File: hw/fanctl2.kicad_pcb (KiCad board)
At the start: 2 copper layers, 80 x 64.8 mm, 0 parts

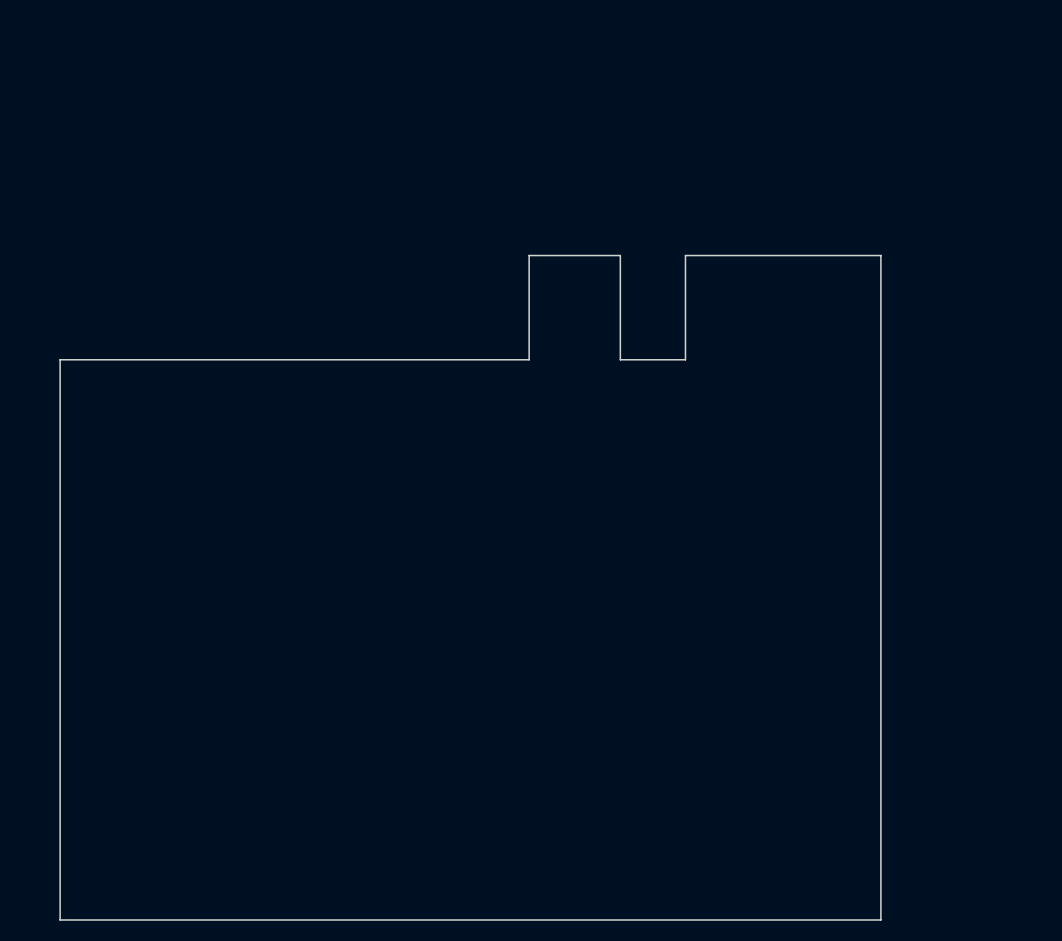
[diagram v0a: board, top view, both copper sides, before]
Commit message: PCB pretty much done.
I changed the size so it would be smaller than 10x10 cm, otherwise it's
absurdly expensive to have it made.
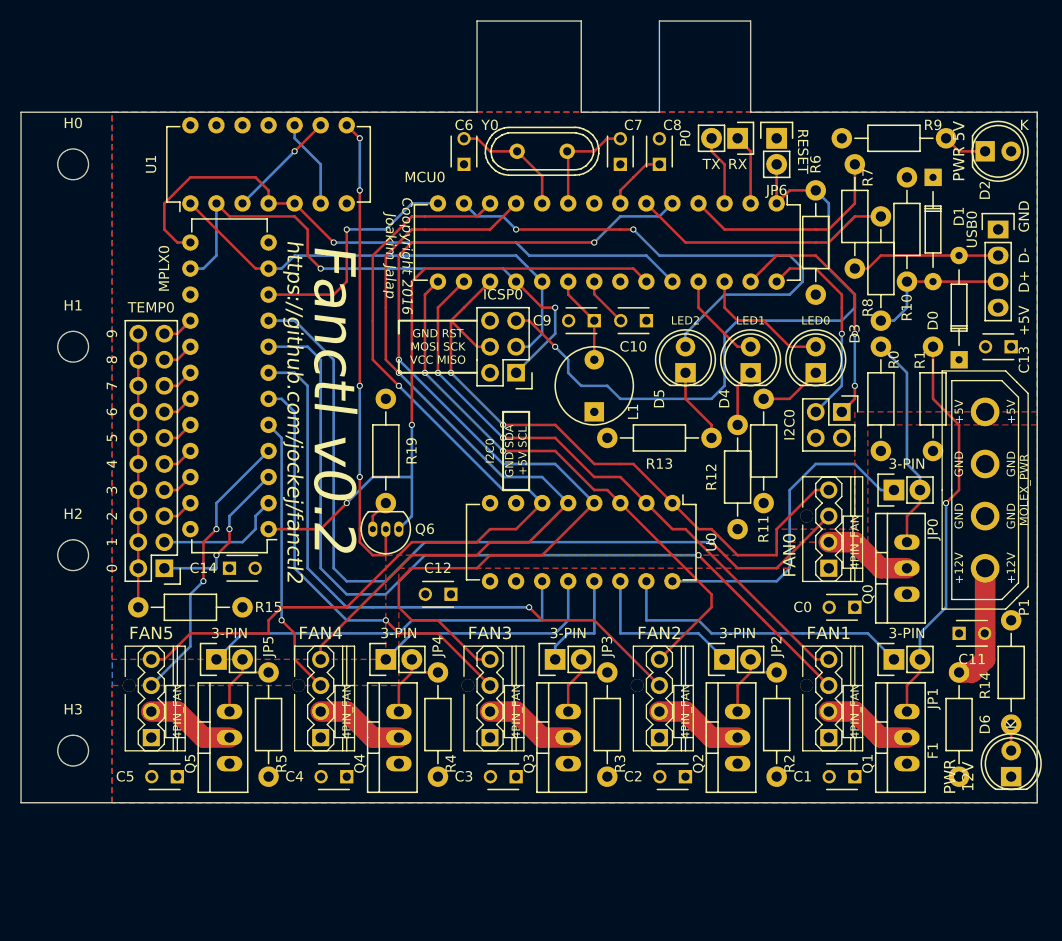
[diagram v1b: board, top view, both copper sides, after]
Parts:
- added C0: Decoupler, Capacitors_ThroughHole:C_Disc_D3_P2.5, F.Cu at (133.3, 130.8)
- added C1: Decoupler, Capacitors_ThroughHole:C_Disc_D3_P2.5, F.Cu at (133.3, 147.3)
- added C10: Decoupler, Capacitors_ThroughHole:C_Disc_D3_P2.5, F.Cu at (113.0, 102.9)
- added C11: Decoupler, Capacitors_ThroughHole:C_Disc_D3_P2.5, F.Cu at (143.5, 133.3)
- added C12: Decoupler, Capacitors_ThroughHole:C_Disc_D3_P2.5, F.Cu at (94.0, 129.5)
- added C13: Decoupler, Capacitors_ThroughHole:C_Disc_D3_P2.5, F.Cu at (148.6, 105.4)
- added C14: Decoupler, Capacitors_ThroughHole:C_Disc_D3_P2.5, F.Cu at (72.4, 127.0)
- added C2: Decoupler, Capacitors_ThroughHole:C_Disc_D3_P2.5, F.Cu at (116.8, 147.3)
- added C3: Decoupler, Capacitors_ThroughHole:C_Disc_D3_P2.5, F.Cu at (100.3, 147.3)
- added C4: Decoupler, Capacitors_ThroughHole:C_Disc_D3_P2.5, F.Cu at (83.8, 147.3)
- added C5: Decoupler, Capacitors_ThroughHole:C_Disc_D3_P2.5, F.Cu at (67.3, 147.3)
- added C6: Decoupler, Capacitors_ThroughHole:C_Disc_D3_P2.5, F.Cu at (95.2, 87.6)
- added C7: Decoupler, Capacitors_ThroughHole:C_Disc_D3_P2.5, F.Cu at (110.5, 87.6)
- added C8: Decoupler, Capacitors_ThroughHole:C_Disc_D3_P2.5, F.Cu at (114.3, 87.6)
- added C9: Decoupler, Capacitors_ThroughHole:C_Disc_D3_P2.5, F.Cu at (108.0, 102.9)
- added D0: ZENER, Diodes_ThroughHole:Diode_DO-35_SOD27_Horizontal_RM10, F.Cu at (143.5, 106.7)
- added D1: ZENER, Diodes_ThroughHole:Diode_DO-35_SOD27_Horizontal_RM10, F.Cu at (141.0, 88.9)
- added D2: LED, LEDs:LED-5MM, F.Cu at (146.1, 86.4)
- added D3: LED, LEDs:LED-5MM, F.Cu at (129.5, 108.0)
- added D4: LED, LEDs:LED-5MM, F.Cu at (123.2, 108.0)
- added D5: LED, LEDs:LED-5MM, F.Cu at (116.8, 108.0)
- added D6: LED, LEDs:LED-5MM, F.Cu at (148.6, 147.3)
- added F1: F_Small, Resistors_ThroughHole:Resistor_Horizontal_RM10mm, F.Cu at (143.5, 142.2)
- added FAN0: 4PIN_FAN, ab2_header:AB2_HDR_M04-1V_CPU_FAN, F.Cu at (130.8, 123.2)
- added FAN1: 4PIN_FAN, ab2_header:AB2_HDR_M04-1V_CPU_FAN, F.Cu at (130.8, 139.7)
- added FAN2: 4PIN_FAN, ab2_header:AB2_HDR_M04-1V_CPU_FAN, F.Cu at (114.3, 139.7)
- added FAN3: 4PIN_FAN, ab2_header:AB2_HDR_M04-1V_CPU_FAN, F.Cu at (97.8, 139.7)
- added FAN4: 4PIN_FAN, ab2_header:AB2_HDR_M04-1V_CPU_FAN, F.Cu at (81.3, 139.7)
- added FAN5: 4PIN_FAN, ab2_header:AB2_HDR_M04-1V_CPU_FAN, F.Cu at (64.8, 139.7)
- added H0: MountingHole_3mm, Mounting_Holes:MountingHole_3mm, F.Cu at (57.1, 87.6)
- added H1: MountingHole_3mm, Mounting_Holes:MountingHole_3mm, F.Cu at (57.1, 105.4)
- added H2: MountingHole_3mm, Mounting_Holes:MountingHole_3mm, F.Cu at (57.1, 125.7)
- added H3: MountingHole_3mm, Mounting_Holes:MountingHole_3mm, F.Cu at (57.1, 144.8)
- added I2C0: I2C_HDR, Pin_Headers:Pin_Header_Straight_2x02, F.Cu at (132.1, 111.8)
- added ICSP0: Prog_con, Pin_Headers:Pin_Header_Straight_2x03, F.Cu at (100.3, 108.0)
- added JP0: Jumper_NC_Small, Pin_Headers:Pin_Header_Straight_1x02, F.Cu at (137.2, 119.4)
- added JP1: Jumper_NC_Small, Pin_Headers:Pin_Header_Straight_1x02, F.Cu at (137.2, 135.9)
- added JP2: Jumper_NC_Small, Pin_Headers:Pin_Header_Straight_1x02, F.Cu at (120.7, 135.9)
- added JP3: Jumper_NC_Small, Pin_Headers:Pin_Header_Straight_1x02, F.Cu at (104.1, 135.9)
- added JP4: Jumper_NC_Small, Pin_Headers:Pin_Header_Straight_1x02, F.Cu at (87.6, 135.9)
- added JP5: Jumper_NC_Small, Pin_Headers:Pin_Header_Straight_1x02, F.Cu at (71.1, 135.9)
- added JP6: Jumper_NO_Small, Pin_Headers:Pin_Header_Straight_1x02, F.Cu at (125.7, 85.1)
- added L1: INDUCTOR_SMALL, Inductors:INDUCTOR_V, F.Cu at (108.0, 109.2)
- added MCU0: ATMEGA168PA-P, Housings_DIP:DIP-28_W7.62mm, F.Cu at (125.7, 91.4)
- added MPLX0: Multiplexer_16:1, Housings_DIP:DIP-24_W7.62mm, F.Cu at (76.2, 123.2)
- added P0: CONN_01X02, Pin_Headers:Pin_Header_Straight_1x02, F.Cu at (121.9, 85.1)
- added P1: MOLEX_PWR, ab2_power:AB2_ATX_PSU-4PIN-V, F.Cu at (146.1, 119.4)
- added Q0: FAN_PMOS, TO_SOT_Packages_THT:TO-220_Neutral123_Vertical, F.Cu at (138.4, 127.0)
- added Q1: FAN_PMOS, TO_SOT_Packages_THT:TO-220_Neutral123_Vertical, F.Cu at (138.4, 143.5)
- added Q2: FAN_PMOS, TO_SOT_Packages_THT:TO-220_Neutral123_Vertical, F.Cu at (121.9, 143.5)
- added Q3: FAN_PMOS, TO_SOT_Packages_THT:TO-220_Neutral123_Vertical, F.Cu at (105.4, 143.5)
- added Q4: FAN_PMOS, TO_SOT_Packages_THT:TO-220_Neutral123_Vertical, F.Cu at (88.9, 143.5)
- added Q5: FAN_PMOS, TO_SOT_Packages_THT:TO-220_Neutral123_Vertical, F.Cu at (72.4, 143.5)
- added Q6: BC413, TO_SOT_Packages_THT:TO-92_Inline_Narrow_Oval, F.Cu at (88.9, 123.2)
- added R0: FANCTL2_R, Resistors_ThroughHole:Resistor_Horizontal_RM10mm, F.Cu at (135.9, 110.5)
- added R1: FANCTL2_R, Resistors_ThroughHole:Resistor_Horizontal_RM10mm, F.Cu at (141.0, 110.5)
- added R10: FANCTL2_R, Resistors_ThroughHole:Resistor_Horizontal_RM10mm, F.Cu at (138.4, 94.0)
- added R11: FANCTL2_R, Resistors_ThroughHole:Resistor_Horizontal_RM10mm, F.Cu at (124.5, 115.6)
- added R12: FANCTL2_R, Resistors_ThroughHole:Resistor_Horizontal_RM10mm, F.Cu at (121.9, 118.1)
- added R13: FANCTL2_R, Resistors_ThroughHole:Resistor_Horizontal_RM10mm, F.Cu at (114.3, 114.3)
- added R14: FANCTL2_R, Resistors_ThroughHole:Resistor_Horizontal_RM10mm, F.Cu at (148.6, 137.2)
- added R15: FANCTL2_R, Resistors_ThroughHole:Resistor_Horizontal_RM10mm, F.Cu at (68.6, 130.8)
- added R19: FANCTL2_R, Resistors_ThroughHole:Resistor_Horizontal_RM10mm, F.Cu at (87.6, 115.6)
- added R2: FANCTL2_R, Resistors_ThroughHole:Resistor_Horizontal_RM10mm, F.Cu at (125.7, 142.2)
- added R3: FANCTL2_R, Resistors_ThroughHole:Resistor_Horizontal_RM10mm, F.Cu at (109.2, 142.2)
- added R4: FANCTL2_R, Resistors_ThroughHole:Resistor_Horizontal_RM10mm, F.Cu at (92.7, 142.2)
- added R5: FANCTL2_R, Resistors_ThroughHole:Resistor_Horizontal_RM10mm, F.Cu at (76.2, 142.2)
- added R6: FANCTL2_R, Resistors_ThroughHole:Resistor_Horizontal_RM10mm, F.Cu at (129.5, 95.2)
- added R7: FANCTL2_R, Resistors_ThroughHole:Resistor_Horizontal_RM10mm, F.Cu at (133.3, 92.7)
- added R8: FANCTL2_R, Resistors_ThroughHole:Resistor_Horizontal_RM10mm, F.Cu at (135.9, 97.8)
- added R9: FANCTL2_R, Resistors_ThroughHole:Resistor_Horizontal_RM10mm, F.Cu at (137.2, 85.1)
- added TEMP0: TMP_SNSR_HDR, Pin_Headers:Pin_Header_Straight_2x10, F.Cu at (66.0, 127.0)
- added U0: ULN2003, Housings_DIP:DIP-16_W7.62mm, F.Cu at (115.6, 120.7)
- added U1: 7400, Housings_DIP:DIP-14_W7.62mm, F.Cu at (68.6, 91.4)
- added USB0: USB_HDR, Pin_Headers:Pin_Header_Straight_1x04, F.Cu at (147.3, 94.0)
- added Y0: Crystal_Small, Crystals:Crystal_HC49-U_Vertical, F.Cu at (102.9, 86.4)
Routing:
- net PWM3: track 0.00 -> 99.5 mm, vias 0 -> 2
- net PWM5: track 0.00 -> 91.1 mm, vias 0 -> 1
- net TACH1: track 0.00 -> 83.3 mm, vias 0 -> 1
- net TACH0: track 0.00 -> 81.8 mm, vias 0 -> 1
- net PWM4: track 0.00 -> 79.7 mm, vias 0 -> 1
- net Net-(ICSP0-Pad5): track 0.00 -> 64.7 mm, vias 0 -> 1
- net SENS0: track 0.00 -> 64.6 mm, vias 0 -> 2
- net PWM0: track 0.00 -> 63.6 mm, vias 0 -> 2
- net TACH2: track 0.00 -> 61.1 mm, vias 0 -> 1
- net SEL3: track 0.00 -> 61.1 mm, vias 0 -> 1
- net PWM1: track 0.00 -> 59.6 mm, vias 0 -> 2
- net SEL2: track 0.00 -> 54.8 mm, vias 0 -> 2
- net PWM2: track 0.00 -> 54.8 mm, vias 0 -> 2
- net LED2: track 0.00 -> 51.7 mm, vias 0 -> 2
- net Net-(Q6-Pad2): track 0.00 -> 46.8 mm, vias 0 -> 4
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- added copper zone on F.Cu, net +12V
- added copper zone on F.Cu, net +5V
- added copper zone on B.Cu, net GND
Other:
- board size 80 x 64.8 mm -> 99.1 x 76.2 mm
- net class fanpwr added: clearance 0.2, trace_width 2, via_dia 0.8, via_drill 0.5
- rule pad_to_mask_clearance: 0.2 -> 0
- board text added: "+5V"
- board text added: "0"
- board text added: "1"
- board text added: "2"
- board text added: "3"
- board text added: "3-PIN"
- board text added: "4"
- board text added: "5"
- board text added: "6"
- board text added: "7"
- board text added: "8"
- board text added: "9"
- board text added: "Coopyright 2016 Joakim Jalap"
- board text added: "D+"
- board text added: "D-"
- board text added: "Fanctl v0.2"
- board text added: "GND"
- board text added: "GND RST MOSI SCK VCC MISO"
- board text added: "GND SDA +5V SCL"
- board text added: "I2C0"
- board text added: "LED0"
- board text added: "LED1"
- board text added: "LED2"
- board text added: "PWR 12V"
- board text added: "PWR 5V"
- board text added: "RESET"
- board text added: "RX"
- board text added: "TX"
- board text added: "https://github.com/jockej/fanctl2"

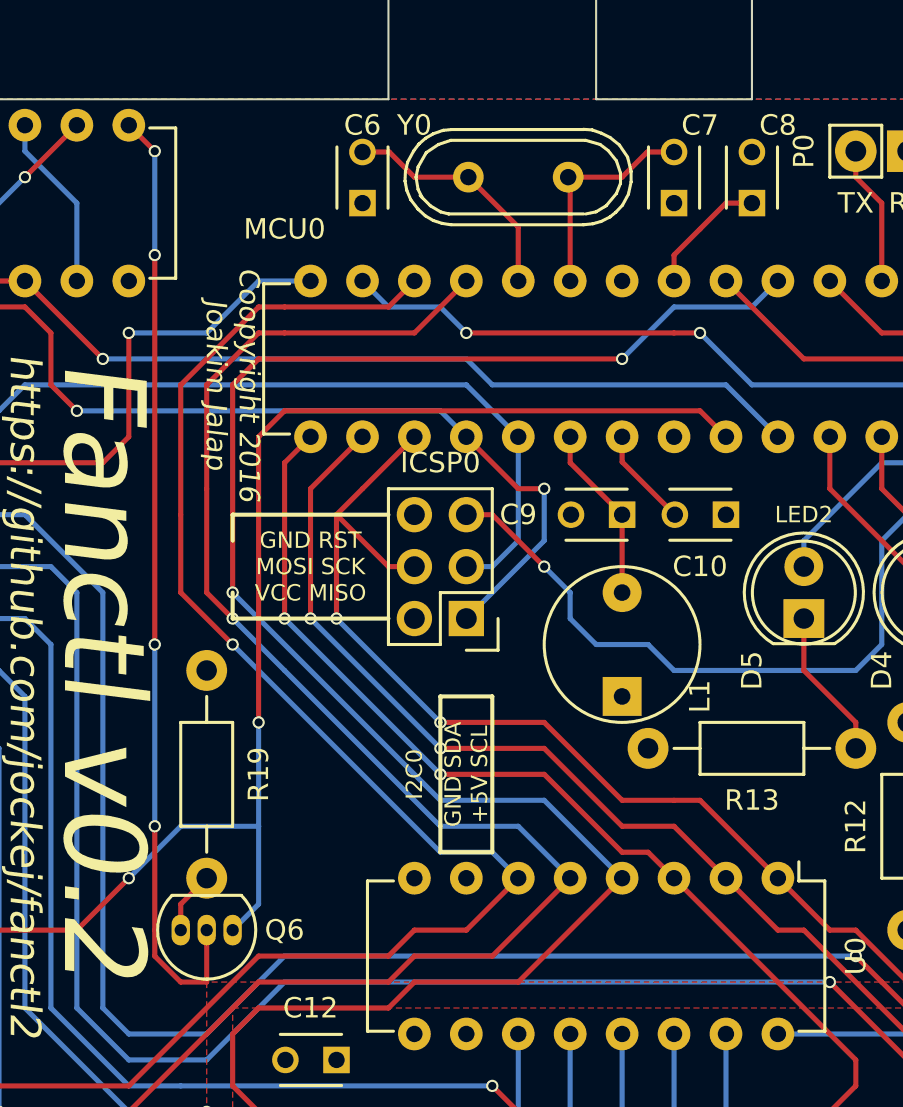
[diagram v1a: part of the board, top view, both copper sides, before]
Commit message: Add a resistor.
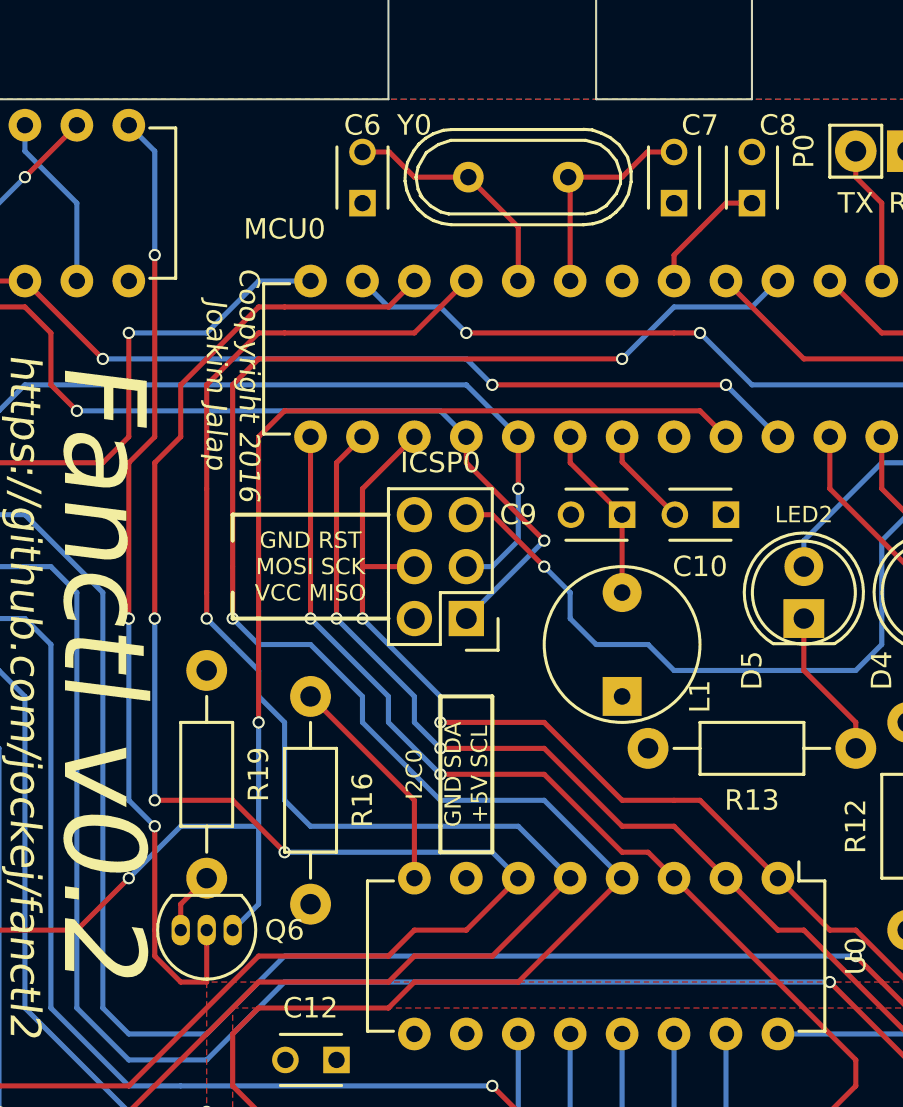
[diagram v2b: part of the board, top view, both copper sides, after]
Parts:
- added R16: R, Resistors_ThroughHole:Resistor_Horizontal_RM10mm, F.Cu at (92.7, 116.8)
- U0: value ULN2003 -> F2_ULN2003
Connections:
- U0 pad 8: GND -> Net-(R16-Pad1)
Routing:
- net Net-(R16-Pad1): track 0.00 -> 11.0 mm
- net PWM5: track 91.1 -> 98.9 mm, vias 1 -> 3
- net PWM4: track 79.7 -> 83.4 mm
- net PWM0: track 63.6 -> 60.3 mm
- net PWM3: track 99.5 -> 101.0 mm
- net PWM1: track 59.6 -> 58.6 mm
- net Net-(Q6-Pad2): track 46.8 -> 47.8 mm, vias 4 -> 3
- net PWM2: track 54.8 -> 53.7 mm
- net SEL2: track 54.8 -> 54.0 mm
- net SEL3: vias 1 -> 3
- net SEL1: vias 0 -> 1

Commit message: Tons of changes
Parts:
- removed Q0: FAN_PMOS, TO_SOT_Packages_THT:TO-220_Neutral123_Vertical
- removed R0: FANCTL2_R, Resistors_ThroughHole:Resistor_Horizontal_RM10mm
- removed TEMP0: TMP_SNSR_HDR, Pin_Headers:Pin_Header_Straight_2x10
- removed U0: F2_ULN2003, Housings_DIP:DIP-16_W7.62mm
- added C15: 22n, Capacitors_ThroughHole:C_Disc_D3_P2.5, F.Cu at (107.3, 87.0)
- added D10: LED, LEDs:LED-5MM, F.Cu at (62.9, 86.4)
- added D11: ZENER, Diodes_ThroughHole:Diode_DO-35_SOD27_Horizontal_RM10, F.Cu at (139.7, 94.6)
- added D12: ZENER, Diodes_ThroughHole:Diode_DO-35_SOD27_Horizontal_RM10, F.Cu at (137.8, 88.9)
- added D7: LED, LEDs:LED-5MM, F.Cu at (142.9, 85.7)
- added D8: LED, LEDs:LED-5MM, F.Cu at (62.9, 101.0)
- added D9: LED, LEDs:LED-5MM, F.Cu at (62.9, 94.0)
- added JP10: JUMPER3, Pin_Headers:Pin_Header_Straight_1x03, F.Cu at (67.3, 132.1)
- added JP11: JUMPER3, Pin_Headers:Pin_Header_Straight_1x03, F.Cu at (62.2, 135.9)
- added JP12: Jumper_NO_Small, Pin_Headers:Pin_Header_Straight_1x02, F.Cu at (120.7, 84.5)
- added JP7: JUMPER3, Pin_Headers:Pin_Header_Straight_1x03, F.Cu at (88.9, 135.9)
- added JP8: JUMPER3, Pin_Headers:Pin_Header_Straight_1x03, F.Cu at (80.6, 132.1)
- added JP9: JUMPER3, Pin_Headers:Pin_Header_Straight_1x03, F.Cu at (75.6, 135.9)
- added P2: CONN_01X04, Pin_Headers:Pin_Header_Straight_1x04, F.Cu at (129.5, 119.4)
- added P3: CONN_01X04, Pin_Headers:Pin_Header_Straight_1x04, F.Cu at (137.2, 119.4)
- added P4: CONN_01X04, Pin_Headers:Pin_Header_Straight_1x04, F.Cu at (133.3, 119.4)
- added Q7: FAN_NMOS, TO_SOT_Packages_THT:TO-220_Neutral123_Vertical, F.Cu at (132.7, 141.0)
- added R17: FANCTL2_R, Resistors_ThroughHole:Resistor_Horizontal_RM10mm, F.Cu at (137.8, 110.5)
- added R18: FANCTL2_R, Resistors_ThroughHole:Resistor_Horizontal_RM10mm, F.Cu at (134.6, 110.5)
- added R20: FANCTL2_R, Resistors_ThroughHole:Resistor_Horizontal_RM10mm, F.Cu at (123.2, 121.9)
- added R21: FANCTL2_R, Resistors_ThroughHole:Resistor_Horizontal_RM10mm, F.Cu at (77.5, 99.1)
- added R22: FANCTL2_R, Resistors_ThroughHole:Resistor_Horizontal_RM10mm, F.Cu at (74.9, 101.0)
- added RR1: RR8, Housings_SIP:SIP9_Housing, F.Cu at (83.2, 115.6)
- added TEMP1: TMP_SNSR_HDR, Pin_Headers:Pin_Header_Straight_2x08, F.Cu at (73.0, 111.8)
- added U2: LM358, Housings_DIP:DIP-8_W7.62mm, F.Cu at (124.5, 99.7)
- added U3: P82B96, Housings_DIP:DIP-8_W7.62mm, F.Cu at (112.4, 118.1)
- C0, C1, C13, C14, C2, C3, C4, C5, C8, C9: value Decoupler -> 0.1u
- C10, C12: value Decoupler -> C
- C6, C7: value Decoupler -> 22p
- D0, D1: value ZENER -> D
- D2, D3, D4, D5: value LED -> D; footprint LEDs:LED-5MM -> Diodes_ThroughHole:Diode_DO-35_SOD27_Horizontal_RM10
- JP0, JP1, JP2, JP3, JP4, JP5: value Jumper_NC_Small -> JUMPER3; footprint Pin_Headers:Pin_Header_Straight_1x02 -> Pin_Headers:Pin_Header_Straight_1x03
- JP6: value Jumper_NO_Small -> JUMPER3; footprint Pin_Headers:Pin_Header_Straight_1x02 -> Pin_Headers:Pin_Header_Straight_1x03
- L1: value INDUCTOR_SMALL -> 10uH
- P0: value CONN_01X02 -> CONN_01X03; footprint Pin_Headers:Pin_Header_Straight_1x02 -> Pin_Headers:Pin_Header_Straight_1x03
- Q1, Q2, Q3, Q4, Q5: value FAN_PMOS -> FAN_NMOS
- R1, R6: value FANCTL2_R -> 10K
- R16: value R -> FANCTL2_R
- R2, R4: value FANCTL2_R -> 10k
- R3, R5: value FANCTL2_R -> R
- R7, R8: value FANCTL2_R -> 68
- moved R1 79.9 mm to (62.2, 123.8), turned to 270 degrees
- moved R5 75.1 mm to (139.7, 102.2), turned to 0 degrees
- moved C5 71.8 mm to (139.1, 148.0), turned to 90 degrees
- moved R15 68.4 mm to (127.0, 95.2), turned to 0 degrees
- moved D2 65.5 mm to (113.0, 142.9), turned to 90 degrees
- moved C0 63.3 mm to (72.4, 148.0), turned to 90 degrees
- moved R11 62.4 mm to (62.2, 110.5)
- moved R12 58.3 mm to (71.1, 89.5), turned to 270 degrees
- moved JP6 56.7 mm to (94.0, 132.1), turned to 270 degrees
- moved D5 56.0 mm to (73.0, 142.9)
- moved D1 55.9 mm to (126.4, 142.9), turned to 90 degrees
- moved R13 52.0 mm to (68.6, 89.5), turned to 90 degrees
- moved D4 50.8 mm to (86.4, 142.9)
- moved I2C0 47.8 mm to (85.1, 102.9)
- moved C1 47.6 mm to (85.7, 148.0), turned to 90 degrees
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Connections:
- C0 pad 2: GND -> 12VGND
- C1 pad 2: GND -> 12VGND
- C10 pad 1: GND -> I5V
- C11 pad 1: GND -> 12VGND
- C12 pad 1: +12V -> Net-(C12-Pad1)
- C12 pad 2: GND -> I12V
- C13 pad 1: +5V -> Net-(C13-Pad1)
- C2 pad 2: GND -> 12VGND
- C3 pad 2: GND -> 12VGND
- C4 pad 2: GND -> 12VGND
- C5 pad 2: GND -> 12VGND
- D0 pad 1: GND -> Net-(D0-Pad1)
- D0 pad 2: Net-(D0-Pad2) -> 12VGND
- D1 pad 1: GND -> Net-(D1-Pad1)
- D1 pad 2: Net-(D1-Pad2) -> 12VGND
- D2 pad 2: +5V -> 12VGND
- D3 pad 2: LED0 -> 12VGND
- D4 pad 2: LED1 -> 12VGND
- D5 pad 2: LED2 -> 12VGND
- D6 pad 1: GND -> 12VGND
- FAN0 pad 1: GND -> 12VGND
- FAN0 pad 2: Net-(FAN0-Pad2) -> Net-(D0-Pad1)
- FAN0 pad 4: PWM0 -> Net-(FAN0-Pad4)
- FAN1 pad 1: GND -> 12VGND
- FAN1 pad 2: Net-(FAN1-Pad2) -> Net-(D1-Pad1)
- FAN1 pad 4: PWM1 -> Net-(FAN1-Pad4)
- FAN2 pad 1: GND -> 12VGND
- FAN2 pad 2: Net-(FAN2-Pad2) -> Net-(D2-Pad1)
- FAN2 pad 4: PWM2 -> Net-(FAN2-Pad4)
- FAN3 pad 1: GND -> 12VGND
- FAN3 pad 2: Net-(FAN3-Pad2) -> Net-(D3-Pad1)
- FAN3 pad 4: PWM3 -> Net-(FAN3-Pad4)
- FAN4 pad 1: GND -> 12VGND
- FAN4 pad 2: Net-(FAN4-Pad2) -> Net-(D4-Pad1)
- FAN4 pad 4: PWM4 -> Net-(FAN4-Pad4)
- FAN5 pad 1: GND -> 12VGND
- FAN5 pad 2: Net-(FAN5-Pad2) -> Net-(D5-Pad1)
- FAN5 pad 4: PWM5 -> Net-(FAN5-Pad4)
- I2C0 pad 1: Net-(I2C0-Pad1) -> SCL
- I2C0 pad 3: Net-(I2C0-Pad3) -> SDA
- JP0 pad 1: PWM12_0 -> COM5V
- JP0 pad 2: Net-(JP0-Pad2) -> Net-(FAN0-Pad4)
- JP1 pad 1: PWM12_1 -> PWM0
- JP2 pad 1: PWM12_2 -> COM5V
- JP2 pad 2: Net-(JP2-Pad2) -> Net-(FAN1-Pad4)
- JP3 pad 1: PWM12_3 -> PWM1
- JP4 pad 1: PWM12_4 -> COM5V
- JP4 pad 2: Net-(JP4-Pad2) -> Net-(FAN2-Pad4)
- JP5 pad 1: PWM12_5 -> PWM2
- JP6 pad 1: GND -> COM5V
- JP6 pad 2: Net-(ICSP0-Pad5) -> Net-(FAN3-Pad4)
- MCU0 pad 21: Net-(C10-Pad2) -> Net-(C9-Pad1)
- MCU0 pad 27: Net-(I2C0-Pad1) -> SDA
- MCU0 pad 28: Net-(I2C0-Pad3) -> SCL
- MPLX0 pad 16: Net-(MPLX0-Pad16) -> I12V
- MPLX0 pad 17: Net-(MPLX0-Pad17) -> I5V
- P0 pad 1: Net-(MCU0-Pad2) -> Net-(MCU0-Pad3)
- P0 pad 2: Net-(MCU0-Pad3) -> Net-(MCU0-Pad2)
- Q1 pad 1: +12V -> Net-(D1-Pad1)
- Q1 pad 2: Net-(FAN1-Pad2) -> +12V
- Q1 pad 3: Net-(JP1-Pad2) -> Net-(JP3-Pad2)
- Q2 pad 1: +12V -> Net-(D2-Pad1)
- Q2 pad 2: Net-(FAN2-Pad2) -> +12V
- Q2 pad 3: Net-(JP2-Pad2) -> Net-(JP5-Pad2)
- Q3 pad 1: +12V -> Net-(D3-Pad1)
- Q3 pad 2: Net-(FAN3-Pad2) -> +12V
- Q3 pad 3: Net-(JP3-Pad2) -> Net-(JP7-Pad2)
- Q4 pad 1: +12V -> Net-(D4-Pad1)
- Q4 pad 2: Net-(FAN4-Pad2) -> +12V
- Q4 pad 3: Net-(JP4-Pad2) -> Net-(JP9-Pad2)
- Q5 pad 1: +12V -> Net-(D5-Pad1)
- Q5 pad 2: Net-(FAN5-Pad2) -> +12V
- Q5 pad 3: Net-(JP5-Pad2) -> Net-(JP11-Pad2)
- Q6 pad 1: SENS0 -> +5V
- R1 pad 1: +12V -> +5V
- R1 pad 2: Net-(JP1-Pad2) -> COM5V
- R10 pad 1: Net-(D1-Pad2) -> Net-(D11-Pad1)
- R11 pad 2: Net-(D3-Pad1) -> Net-(D8-Pad1)
- R12 pad 2: Net-(D4-Pad1) -> Net-(D9-Pad1)
- R13 pad 2: Net-(D5-Pad1) -> Net-(D10-Pad1)
- R15 pad 1: +5V -> Net-(C10-Pad2)
- R15 pad 2: Net-(R15-Pad2) -> +5V
- R16 pad 1: Net-(R16-Pad1) -> I5V
- R16 pad 2: GND -> Net-(C10-Pad2)
- R19 pad 1: Net-(Q6-Pad3) -> Net-(P2-Pad3)
- R19 pad 2: GND -> +12V
- R2 pad 1: +12V -> +5V
- R2 pad 2: Net-(JP2-Pad2) -> Net-(MPLX0-Pad15)
- R3 pad 1: +12V -> GND
- R3 pad 2: Net-(JP3-Pad2) -> 12VGND
- R4 pad 1: +12V -> GND
- R4 pad 2: Net-(JP4-Pad2) -> Net-(Q6-Pad2)
- R5 pad 1: +12V -> +5V
- R5 pad 2: Net-(JP5-Pad2) -> Net-(C13-Pad1)
- R7 pad 1: Net-(D0-Pad2) -> Net-(D12-Pad1)
- R8 pad 1: Net-(D1-Pad2) -> Net-(D11-Pad1)
- R9 pad 1: Net-(D2-Pad1) -> Net-(D7-Pad1)
- U1 pad 10: Net-(U1-Pad10) -> SEL3
- U1 pad 14: +5V -> VCC
- U1 pad 4: SEL3 -> Net-(U1-Pad3)
- U1 pad 5: SEL3 -> Net-(U1-Pad3)
- U1 pad 6: Net-(U1-Pad10) -> Net-(U1-Pad6)
- U1 pad 9: Net-(U1-Pad3) -> Net-(U1-Pad6)
- USB0 pad 2: Net-(D0-Pad2) -> Net-(D12-Pad1)
- USB0 pad 3: Net-(D1-Pad2) -> Net-(D11-Pad1)
- USB0 pad 4: +5V -> Net-(C13-Pad1)
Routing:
- net PWM0: track 60.3 -> 133.8 mm, vias 2 -> 3
- net SCL: track 0.00 -> 65.6 mm, vias 0 -> 2
- net SDA: track 0.00 -> 60.8 mm, vias 0 -> 2
- net SEL0: track 23.2 -> 75.1 mm, vias 1 -> 5
- net I12V: track 0.00 -> 49.7 mm, vias 0 -> 3
- net I5V: track 0.00 -> 45.2 mm, vias 0 -> 3
- net +5V: track 6.13 -> 49.2 mm, vias 0 -> 1
- net PWM5: track 98.9 -> 60.4 mm, vias 3 -> 1
- net LED0: track 13.0 -> 51.2 mm, vias 0 -> 2
- net TACH1: track 83.3 -> 45.3 mm
- net LED1: track 9.20 -> 46.5 mm, vias 0 -> 2
- net PWM12_5: track 37.1 -> 0.00 mm
- net PWM1: track 58.6 -> 94.5 mm, vias 2 -> 1
- net Net-(JP1-Pad2): track 38.7 -> 6.66 mm, vias 1 -> 0
- net PWM12_0: track 31.8 -> 0.00 mm
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- added copper zone on B.Cu, net 12VGND
- added copper zone on F.Cu, net COM5V
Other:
- board size 99.1 x 76.2 mm -> 95.9 x 76.2 mm
- board text added: "+5V SCL"
- board text added: "GND SDA"
- board text added: "github.com/jockej/fanctl2"
- board text removed: "0"
- board text removed: "1"
- board text removed: "2"
- board text removed: "3"
- board text removed: "3-PIN"
- board text removed: "4"
- board text removed: "5"
- board text removed: "6"
- board text removed: "7"
- board text removed: "8"
- board text removed: "9"
- board text removed: "Fanctl v0.2"
- board text removed: "GND SDA +5V SCL"
- board text removed: "I2C0"
- board text removed: "PWR 12V"
- board text removed: "PWR 5V"
- board text removed: "https://github.com/jockej/fanctl2"
